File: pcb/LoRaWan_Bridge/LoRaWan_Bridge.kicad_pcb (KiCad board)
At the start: 2 copper layers, 27 x 64.5 mm, 5 parts, among them J1 Conn_01x13, J2 Conn_01x13, J3 Conn_02x04_Odd_Even

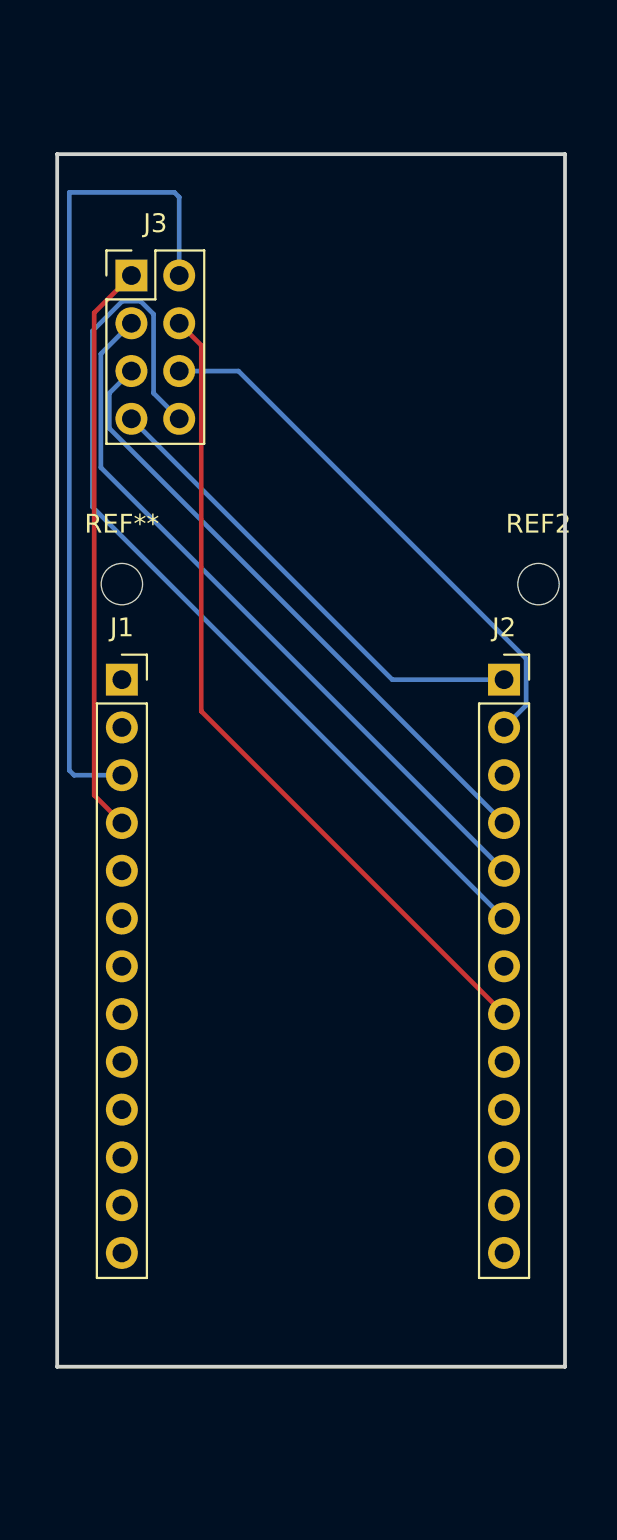
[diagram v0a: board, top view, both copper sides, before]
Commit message: PCB updates to fix pin spacing
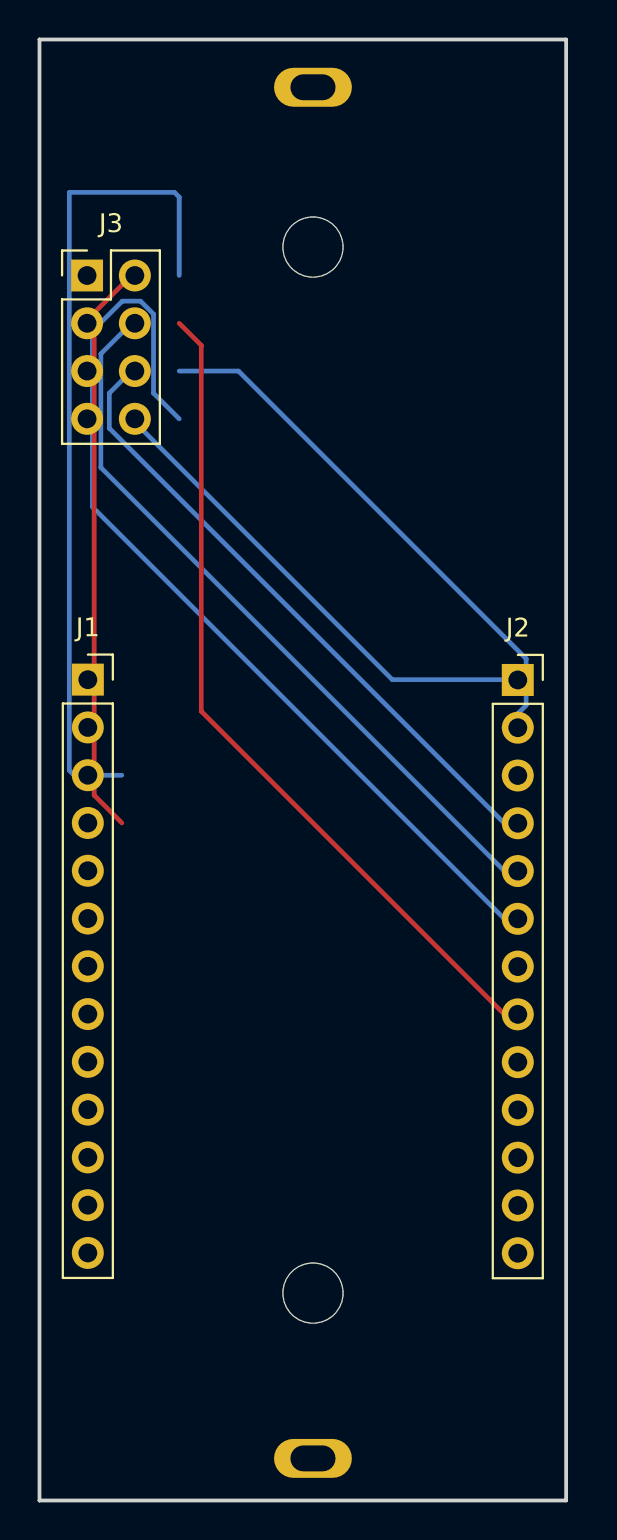
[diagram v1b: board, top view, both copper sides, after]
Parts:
- removed REF**, REF2: MountingHole_2.2mm_M2, MountingHole:MountingHole_2.2mm_M2
- added BT2: BK-18650-PC2, BK-18650-PC2:BAT_BK-18650-PC2, B.Cu at (129.5, 73.4)
- moved J3 2.36 mm to (120.1, 47.1)
- moved J1 1.81 mm to (117.6, 68.6)
- moved J2 0.73 mm to (140.4, 68.6)
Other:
- board size 27 x 64.5 mm -> 28 x 77.7 mm
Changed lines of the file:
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@@
   (net 25 "unconnected-(J2-Pin_12-Pad12)")
   (net 26 "unconnected-(J2-Pin_13-Pad13)")
+  (net 27 "+BATT")
   (footprint "Connector_PinSocket_2.54mm:PinSocket_2x04_P2.54mm_Vertical" (layer "F.Cu")
-    (at 122.468 47.0916)
+    (at 120.11 47.0916)
     (descr "Through hole straight socket strip, 2x04, 2.54mm pitch, double cols (from Kicad 4.0.7), script generated")
     (tags "Through hole socket strip THT 2x04 2.54mm double row")
@@
   )
   (footprint "Connector_PinSocket_2.54mm:PinSocket_1x13_P2.54mm_Vertical" (layer "F.Cu")
-    (at 139.7 68.58)
+    (at 140.43 68.595)
     (descr "Through hole straight socket strip, 1x13, 2.54mm pitch, single row (from Kicad 4.0.7), script generated")
     (tags "Through hole socket strip THT 1x13 2.54mm single row")
@@
     )
   )
-  (footprint "MountingHole:MountingHole_2.2mm_M2" (layer "F.Cu")
-    (at 119.38 63.5)
-    (descr "Mounting Hole 2.2mm, no annular, M2")
-    (tags "mounting hole 2.2mm no annular m2")
-    (attr exclude_from_pos_files exclude_from_bom)
-    (fp_text reference "REF**" (at 0 -3.2) (layer "F.SilkS")
-        (effects (font (size 1 1) (thickness 0.15)))
-    )
-    (fp_text value "MountingHole_2.2mm_M2" (at 0 3.2) (layer "F.Fab")
-        (effects (font (size 1 1) (thickness 0.15)))
-    )
-    (fp_text user "${REFERENCE}" (at 0 0) (layer "F.Fab")
-        (effects (font (size 1 1) (thickness 0.15)))
-    )
-    (fp_circle (center 0 0) (end 2.2 0)
-      (stroke (width 0.15) (type solid)) (fill none) (layer "Cmts.User"))
-    (fp_circle (center 0 0) (end 2.45 0)
-      (stroke (width 0.05) (type solid)) (fill none) (layer "F.CrtYd"))
-    (pad "" np_thru_hole circle (at 0 0) (size 2.2 2.2) (drill 2.2) (layers "*.Cu" "*.Mask"))
-  )
-  (footprint "MountingHole:MountingHole_2.2mm_M2" (layer "F.Cu")
-    (at 141.53 63.5)
-    (descr "Mounting Hole 2.2mm, no annular, M2")
-    (tags "mounting hole 2.2mm no annular m2")
-    (attr exclude_from_pos_files exclude_from_bom)
-    (fp_text reference "REF2" (at 0 -3.2) (layer "F.SilkS")
-        (effects (font (size 1 1) (thickness 0.15)))
-    )
-    (fp_text value "MountingHole_2.2mm_M2" (at 0 3.2) (layer "F.Fab")
-        (effects (font (size 1 1) (thickness 0.15)))
-    )
-    (fp_text user "${REFERENCE}" (at 0 0) (layer "F.Fab")
-        (effects (font (size 1 1) (thickness 0.15)))
-    )
-    (fp_circle (center 0 0) (end 2.2 0)
-      (stroke (width 0.15) (type solid)) (fill none) (layer "Cmts.User"))
-    (fp_circle (center 0 0) (end 2.45 0)
-      (stroke (width 0.05) (type solid)) (fill none) (layer "F.CrtYd"))
-    (pad "" np_thru_hole circle (at 0 0) (size 2.2 2.2) (drill 2.2) (layers "*.Cu" "*.Mask"))
-  )
   (footprint "Connector_PinSocket_2.54mm:PinSocket_1x13_P2.54mm_Vertical" (layer "F.Cu")
-    (at 119.38 68.58)
+    (at 117.57 68.58)
     (descr "Through hole straight socket strip, 1x13, 2.54mm pitch, single row (from Kicad 4.0.7), script generated")
     (tags "Through hole socket strip THT 1x13 2.54mm single row")
@@
     )
   )
-  (gr_rect (start 115.94 40.64) (end 142.94 105.11)
+  (footprint "BK-18650-PC2:BAT_BK-18650-PC2" (layer "B.Cu")
+    (at 129.54 73.384 -90)
+    (property "MANUFACTURER" "MPD")
+    (property "MAXIMUM_PACKAGE_HEIGHT" "21.41 mm")
+    (property "PARTREV" "F")
+    (property "STANDARD" "Manufacturer Recommendations")
+    (property "Sheetfile" "LoRaWan_Bridge.kicad_sch")
+    (property "Sheetname" "")
+    (attr through_hole)
+    (fp_text reference "BT2" (at -35.455 11.43 90) (layer "B.SilkS")
+        (effects (font (size 1 1) (thickness 0.15)) (justify mirror))
+    )
+    (fp_text value "BK-18650-PC2" (at -28.47 -11.51 90) (layer "B.Fab")
+        (effects (font (size 1 1) (thickness 0.15)) (justify mirror))
+    )
+    (fp_line (start -41.63 0) (end -39.63 0)
+      (stroke (width 0.127) (type solid)) (layer "B.SilkS"))
+    (fp_line (start -40.63 1) (end -40.63 -1)
+      (stroke (width 0.127) (type solid)) (layer "B.SilkS"))
+    (fp_line (start -38.48 -10.49) (end -38.48 10.49)
+      (stroke (width 0.127) (type solid)) (layer "B.SilkS"))
+    (fp_line (start -38.48 10.49) (end 38.48 10.49)
+      (stroke (width 0.127) (type solid)) (layer "B.SilkS"))
+    (fp_line (start 38.48 -10.49) (end -38.48 -10.49)
+      (stroke (width 0.127) (type solid)) (layer "B.SilkS"))
+    (fp_line (start 38.48 10.49) (end 38.48 -10.49)
+      (stroke (width 0.127) (type solid)) (layer "B.SilkS"))
+    (fp_line (start 39.63 0) (end 41.63 0)
+      (stroke (width 0.127) (type solid)) (layer "B.SilkS"))
+    (fp_line (start -38.73 -10.74) (end -38.73 10.74)
+      (stroke (width 0.05) (type solid)) (layer "B.CrtYd"))
+    (fp_line (start -38.73 10.74) (end 38.73 10.74)
+      (stroke (width 0.05) (type solid)) (layer "B.CrtYd"))
+    (fp_line (start 38.73 -10.74) (end -38.73 -10.74)
+      (stroke (width 0.05) (type solid)) (layer "B.CrtYd"))
+    (fp_line (start 38.73 10.74) (end 38.73 -10.74)
+      (stroke (width 0.05) (type solid)) (layer "B.CrtYd"))
+    (fp_line (start -41.63 0) (end -39.63 0)
+      (stroke (width 0.127) (type solid)) (layer "B.Fab"))
+    (fp_line (start -40.63 1) (end -40.63 -1)
+      (stroke (width 0.127) (type solid)) (layer "B.Fab"))
+    (fp_line (start -38.48 -10.49) (end -38.48 10.49)
+      (stroke (width 0.127) (type solid)) (layer "B.Fab"))
+    (fp_line (start -38.48 10.49) (end 38.48 10.49)
+      (stroke (width 0.127) (type solid)) (layer "B.Fab"))
+    (fp_line (start 38.48 -10.49) (end -38.48 -10.49)
+      (stroke (width 0.127) (type solid)) (layer "B.Fab"))
+    (fp_line (start 38.48 10.49) (end 38.48 -10.49)
+      (stroke (width 0.127) (type solid)) (layer "B.Fab"))
+    (fp_line (start 39.63 0) (end 41.63 0)
+      (stroke (width 0.127) (type solid)) (layer "B.Fab"))
+    (pad "" np_thru_hole circle (at -27.805 0 270) (size 3.2 3.2) (drill 3.2) (layers "*.Cu" "*.Mask"))
+    (pad "" np_thru_hole circle (at 27.81 0 270) (size 3.2 3.2) (drill 3.2) (layers "*.Cu" "*.Mask"))
+    (pad "+" thru_hole oval (at -36.3 0 270) (size 2.07 4.14) (drill oval 1.38 2.4) (layers "*.Cu" "*.Mask")
+      (net 27 "+BATT") (pintype "passive"))
+    (pad "-" thru_hole oval (at 36.6 0 270) (size 2.07 4.14) (drill oval 1.38 2.4) (layers "*.Cu" "*.Mask")
+      (net 4 "GND") (pintype "passive"))
+  )
+  (gr_rect (start 115 34.544) (end 143 112.222)
     (stroke (width 0.2) (type default)) (fill none) (layer "Edge.Cuts"))
   (segment (start 122.428 42.926) (end 122.428 47.0916) (width 0.25) (layer "B.Cu") (net 3))
